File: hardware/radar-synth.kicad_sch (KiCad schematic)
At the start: 5 parts

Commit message: Completed schematics
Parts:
- removed C1: 10u, Capacitor_SMD:C_0603_1608Metric, symbol Device:C_Small
- removed C2: 10u, Capacitor_SMD:C_0805_2012Metric, symbol Device:C
- removed C3: 470n, Capacitor_SMD:C_0603_1608Metric, symbol Device:C_Small
- removed C4: 10n, Capacitor_SMD:C_0402_1005Metric, symbol Device:C_Small
- removed C5: 100n, Capacitor_SMD:C_0402_1005Metric, symbol Device:C_Small
- added C47, C48: 100n, Capacitor_SMD:C_0402_1005Metric, symbol Device:C_Small
- added D1: LED, LED_SMD:LED_0603_1608Metric, symbol Device:LED
- added D3: PMEG2010ER, Diode_SMD:Nexperia_CFP3_SOD-123W, symbol Diode:PMEG2010ER
- added FB5: 180R, Inductor_SMD:L_0402_1005Metric, symbol Device:FerriteBead_Small
- added J1, J2, J3: Conn_Coaxial_Small, Connector_Coaxial:SMA_Molex_73251-2120_EdgeMount_Horizontal, symbol Connector:Conn_Coaxial_Small
- added J4: Conn_01x04_MountingPin, symbol Connector_Generic_MountingPin:Conn_01x04_MountingPin
- added J5: Conn_01x02_MountingPin, symbol Connector_Generic_MountingPin:Conn_01x02_MountingPin
- added R11: 51R, Resistor_SMD:R_0402_1005Metric, symbol Device:R_Small
- added R13, R14: 49R9, Resistor_SMD:R_0402_1005Metric, symbol Device:R_Small
- added R19: 2K2, Resistor_SMD:R_0402_1005Metric, symbol Device:R_Small
- added R20, R30, R31: 0R, Resistor_SMD:R_0402_1005Metric, symbol Device:R_Small
- added U1: 74AUP1G34, symbol 74xGxx:74AUP1G34
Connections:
- net lmx2572_rf_pll_synth/REF_OSC_N: now also R11.2
- net lmx2572_rf_pll_synth/rf_out_a_n: now also R13.2
- net lmx2572_rf_pll_synth/rf_out_a_p: now also J1.1 (In)
- net lmx2572_rf_pll_synth/rf_out_b_n: now also R14.2
- net lmx2572_rf_pll_synth/rf_out_b_p: now also J2.1 (In)
- new net: J4.3 (Pin_3), R31.1
- new net: R20.2, U1.2
- new net: J4.4 (Pin_4), R30.1
- new net: J5.1 (Pin_1), R20.1
- new net: FB5.1, J4.1 (Pin_1)
- new net: D1.2 (A), R19.2
- new net 3V3: C48.1, R19.1, U1.5 (VCC)
- new net 5V0: D3.1 (K)
- new net 5V0_EXT: C47.2, D3.2 (A), FB5.2
- new net GND: C47.1, C48.2, J1.2 (Ext), J2.2 (Ext), J3.2 (Ext), J4.2 (Pin_2), J5.2 (Pin_2), R11.1, R13.1, R14.1, U1.3 (GND)
- new net controller/LED0: D1.1 (K)
- new net controller/RXD0: R30.2
- new net controller/TXD0: R31.2
- new net lmx2572_rf_pll_synth/pll_sync_ext: U1.4
- new net ref_osc/clk_ext: J3.1 (In)
- no-connect marks 0 -> 3
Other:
- added sheet controller (xia0_esp32s3p_controller.kicad_sch)
- added sheet ref_osc (reference_clock.kicad_sch)
- sheet lmx2572_rf_pll_synth ports: added pll_sync_ext; removed none
- company: (none) -> ${COMPANY}
- title: (none) -> TOP LEVEL

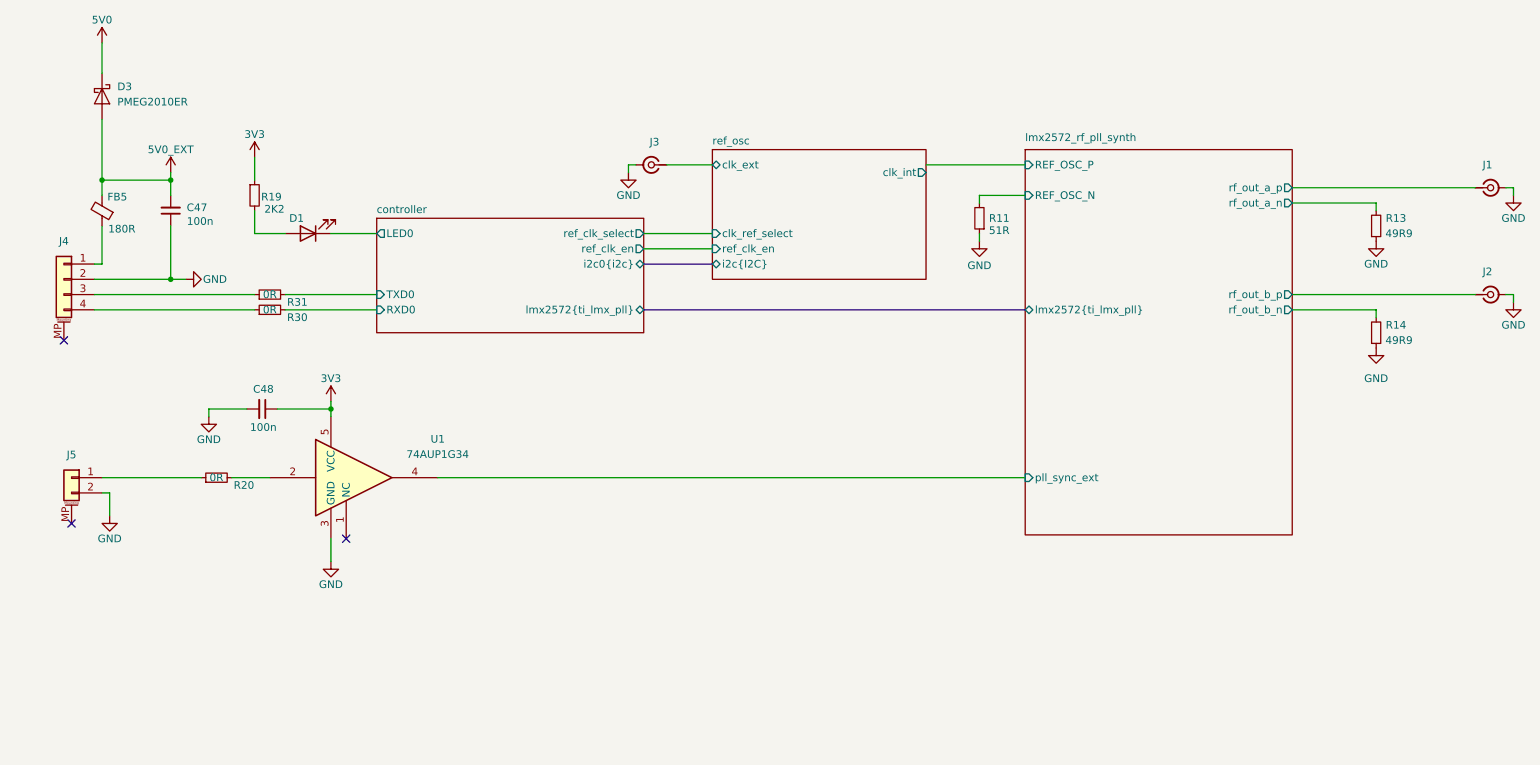
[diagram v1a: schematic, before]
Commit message: Completed core PCB routing
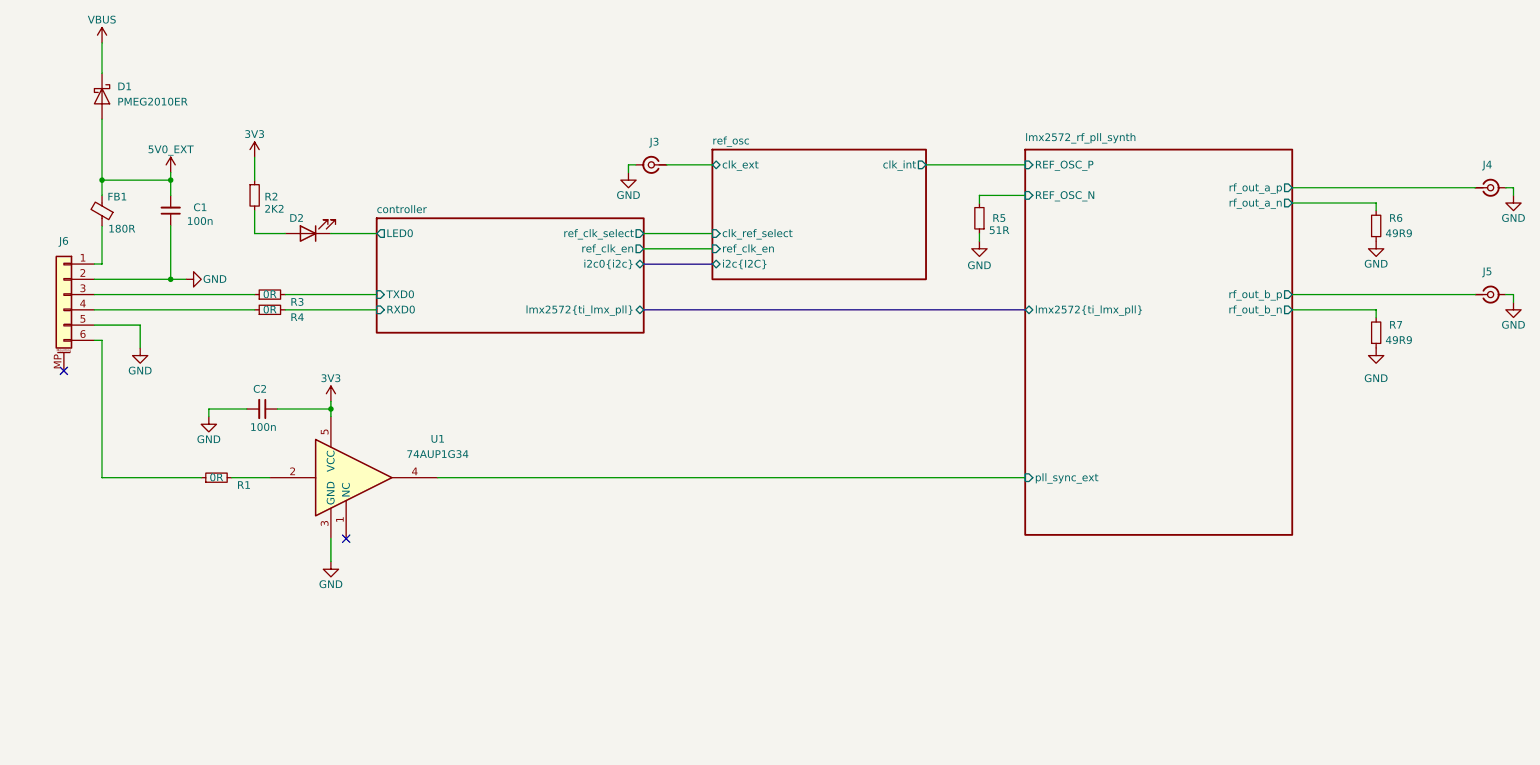
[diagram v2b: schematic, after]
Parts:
- removed J4: Conn_01x04_MountingPin, symbol Connector_Generic_MountingPin:Conn_01x04_MountingPin
- removed J5: Conn_01x02_MountingPin, symbol Connector_Generic_MountingPin:Conn_01x02_MountingPin
- added J6: Conn_01x06_MountingPin, Connector_JST:JST_GH_SM06B-GHS-TB_1x06-1MP_P1.25mm_Horizontal, symbol Connector_Generic_MountingPin:Conn_01x06_MountingPin
- J3: footprint Connector_Coaxial:SMA_Molex_73251-2120_EdgeMount_Horizontal -> Connector_Coaxial:SMA_Samtec_SMA-J-P-H-ST-EM1_EdgeMount
- J4: renamed from J1; footprint Connector_Coaxial:SMA_Molex_73251-2120_EdgeMount_Horizontal -> Connector_Coaxial:SMA_Samtec_SMA-J-P-H-ST-EM1_EdgeMount
- J5: renamed from J2; footprint Connector_Coaxial:SMA_Molex_73251-2120_EdgeMount_Horizontal -> Connector_Coaxial:SMA_Samtec_SMA-J-P-H-ST-EM1_EdgeMount
- U1: footprint (none) -> Package_TO_SOT_SMD:SOT-353_SC-70-5
- renumbered C47 to C1, C48 to C2, D3 to D1, D1 to D2, FB5 to FB1, R20 to R1, R19 to R2, R31 to R3, R30 to R4, R11 to R5, R13 to R6, R14 to R7
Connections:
- net GND: now also J6.2 (Pin_2), J6.5 (Pin_5)
- net at R3.1: now also J6.3 (Pin_3)
- net at R4.1: now also J6.4 (Pin_4)
- net at R1.1: now also J6.6 (Pin_6)
- net at FB1.1: now also J6.1 (Pin_1)
- net 5V0 renamed VBUS
- no-connect marks 3 -> 2

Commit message: Ready for FAB info
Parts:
- added H1, H2, H3, H4: MountingHole, MountingHole:MountingHole_2.7mm_M2.5, symbol Mechanical:MountingHole
- added TP1: TestPoint, TestPoint:TestPoint_THTPad_1.0x1.0mm_Drill0.5mm, symbol Connector:TestPoint
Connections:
- net lmx2572_rf_pll_synth/REF_OSC_P: now also TP1.1
- net J6_5V_EXT: now reaches FB1.1, J6.1 (Pin_1)
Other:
- sheet ref_osc ports: added i2c0{i2c}; removed i2c{I2C}

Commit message: Sent off for quote
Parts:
- D1: MPN (none) -> PMEG2010ER,115; Manufacturer (none) -> Nexperia USA Inc.; SPN (none) -> 1727-5192-1-ND; Supplier (none) -> Digikey
- J3, J4, J5: MPN (none) -> SMA-J-P-H-ST-EM1; Manufacturer (none) -> Samtec Inc.; SPN (none) -> SAM8857-ND; Supplier (none) -> Digikey
- J6: MPN (none) -> SM06B-GHS-TB; SPN (none) -> 455-1568-1-ND; Supplier (none) -> Digikey
- R1: MPN (none) -> ERJ-2GE0R00X
- R5: value 51R -> 49R9; MPN (none) -> RR0510R-49R9-D; Manufacturer Vishay Dale -> Susumu; SPN 71-CRCW0402J-51-E3 -> RR05R49.9DCT-ND; Supplier Mouser -> Digikey
- U1: MPN (none) -> 74AUP1G34SE-7; Manufacturer (none) -> Diodes Incorporated; SPN (none) -> 74AUP1G34SE-7-ND; Supplier (none) -> Digikey
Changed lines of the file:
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@@
 			)
 		)
-		(property "Description" "20V, 1A low Vf MEGA Schottky barrier rectifier, SOD-123W"
+		(property "Description" "DIODE SCHOTTKY 20V 1A SOD123W"
+			(at 35.56 55.88 0)
+			(effects
+				(font
+					(size 1.27 1.27)
+				)
+				(hide yes)
+			)
+		)
+		(property "MPN" "PMEG2010ER,115"
+			(at 35.56 55.88 0)
+			(effects
+				(font
+					(size 1.27 1.27)
+				)
+				(hide yes)
+			)
+		)
+		(property "Manufacturer" "Nexperia USA Inc."
+			(at 35.56 55.88 0)
+			(effects
+				(font
+					(size 1.27 1.27)
+				)
+				(hide yes)
+			)
+		)
+		(property "SPN" "1727-5192-1-ND"
+			(at 35.56 55.88 0)
+			(effects
+				(font
+					(size 1.27 1.27)
+				)
+				(hide yes)
+			)
+		)
+		(property "Supplier" "Digikey"
 			(at 35.56 55.88 0)
 			(effects
@@
 			)
 		)
-		(property "Manufacturer" ""
+		(property "Manufacturer" "Diodes Incorporated"
 			(at 78.74 119.38 0)
 			(effects
@@
 			)
 		)
-		(property "MPN" ""
+		(property "MPN" "74AUP1G34SE-7"
 			(at 78.74 119.38 0)
 			(effects
@@
 			)
 		)
-		(property "Supplier" ""
+		(property "Supplier" "Digikey"
 			(at 78.74 119.38 0)
 			(effects
@@
 			)
 		)
-		(property "SPN" ""
+		(property "SPN" "74AUP1G34SE-7-ND"
 			(at 78.74 119.38 0)
 			(effects
@@
 			)
 		)
-		(property "Description" "Resistor, small symbol"
+		(property "Description" "RES SMD 0 OHM JUMPER 1/10W 0402"
 			(at 54.61 119.38 0)
 			(effects
@@
 		)
 		(property "DATE" ""
+			(at 54.61 119.38 0)
+			(effects
+				(font
+					(size 1.27 1.27)
+				)
+				(hide yes)
+			)
+		)
+		(property "MPN" "ERJ-2GE0R00X"
 			(at 54.61 119.38 0)
 			(effects
@@
 			)
 		)
-		(property "Description" "small coaxial connector (BNC, SMA, SMB, SMC, Cinch/RCA, LEMO, ...)"
+		(property "Description" "CONN SMA JACK STR 50OHM EDGE MNT"
 			(at 266.7 71.12 0)
 			(effects
@@
 			)
 		)
-		(property "Manufacturer" ""
+		(property "Manufacturer" "Samtec Inc."
 			(at 266.7 71.12 0)
 			(effects
@@
 			)
 		)
-		(property "MPN" ""
+		(property "MPN" "SMA-J-P-H-ST-EM1"
 			(at 266.7 71.12 0)
 			(effects
@@
 			)
 		)
-		(property "Supplier" ""
+		(property "Supplier" "Digikey"
 			(at 266.7 71.12 0)
 			(effects
@@
 			)
 		)
-		(property "SPN" ""
+		(property "SPN" "SAM8857-ND"
 			(at 266.7 71.12 0)
 			(effects
@@
 			)
 		)
-		(property "Value" "51R"
+		(property "Value" "49R9"
 			(at 184.912 78.232 0)
 			(effects
@@
 			)
 		)
-		(property "Description" "Resistor, small symbol"
+		(property "Description" "RES SMD 49.9 OHM 0.5% 1/16W 0402"
 			(at 181.61 76.2 0)
 			(effects
@@
 			)
 		)
-		(property "Manufacturer" "Vishay Dale"
+		(property "Manufacturer" "Susumu"
 			(at 181.61 76.2 0)
 			(effects
@@
 			)
 		)
-		(property "Supplier" "Mouser"
+		(property "Supplier" "Digikey"
 			(at 181.61 76.2 0)
 			(effects
@@
 			)
 		)
-		(property "SPN" "71-CRCW0402J-51-E3 "
+		(property "SPN" "RR05R49.9DCT-ND"
 			(at 181.61 76.2 0)
 			(effects
@@
 				)
 				(hide yes)
+			)
+		)
+		(property "MPN" "RR0510R-49R9-D"
+			(at 181.61 76.2 0)
+			(effects
+				(font
+					(size 1.27 1.27)
+				)
 			)
 		)
@@
 			)
 		)
-		(property "Description" "small coaxial connector (BNC, SMA, SMB, SMC, Cinch/RCA, LEMO, ...)"
+		(property "Description" "CONN SMA JACK STR 50OHM EDGE MNT"
 			(at 127 67.31 0)
 			(effects
@@
 			)
 		)
-		(property "Manufacturer" ""
+		(property "Manufacturer" "Samtec Inc."
 			(at 127 67.31 0)
 			(effects
@@
 			)
 		)
-		(property "MPN" ""
+		(property "MPN" "SMA-J-P-H-ST-EM1"
 			(at 127 67.31 0)
 			(effects
@@
 			)
 		)
-		(property "Supplier" ""
+		(property "Supplier" "Digikey"
 			(at 127 67.31 0)
 			(effects
@@
 			)
 		)
-		(property "SPN" ""
+		(property "SPN" "SAM8857-ND"
 			(at 127 67.31 0)
 			(effects
@@
 			)
 		)
-		(property "Description" "Generic connectable mounting pin connector, single row, 01x06, script generated (kicad-library-utils/schlib/autogen/connector/)"
+		(property "Description" "CONN HEADER SMD R/A 6POS 1.25MM"
 			(at 29.21 88.9 0)
 			(effects
@@
 			)
 		)
-		(property "MPN" ""
+		(property "MPN" "SM06B-GHS-TB"
 			(at 29.21 88.9 0)
 			(effects
@@
 			)
 		)
-		(property "Supplier" ""
+		(property "Supplier" "Digikey"
 			(at 29.21 88.9 0)
 			(effects
@@
 			)
 		)
-		(property "SPN" ""
+		(property "SPN" "455-1568-1-ND"
 			(at 29.21 88.9 0)
 			(effects
@@
 			)
 		)
-		(property "Description" "small coaxial connector (BNC, SMA, SMB, SMC, Cinch/RCA, LEMO, ...)"
+		(property "Description" "CONN SMA JACK STR 50OHM EDGE MNT"
 			(at 266.7 88.9 0)
 			(effects
@@
 			)
 		)
-		(property "Manufacturer" ""
+		(property "Manufacturer" "Samtec Inc."
 			(at 266.7 88.9 0)
 			(effects
@@
 			)
 		)
-		(property "MPN" ""
+		(property "MPN" "SMA-J-P-H-ST-EM1"
 			(at 266.7 88.9 0)
 			(effects
@@
 			)
 		)
-		(property "Supplier" ""
+		(property "Supplier" "Digikey"
 			(at 266.7 88.9 0)
 			(effects
@@
 			)
 		)
-		(property "SPN" ""
+		(property "SPN" "SAM8857-ND"
 			(at 266.7 88.9 0)
 			(effects

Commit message: Updated firmware
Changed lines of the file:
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@@
 					(size 1.27 1.27)
 				)
+				(hide yes)
 			)
 		)
